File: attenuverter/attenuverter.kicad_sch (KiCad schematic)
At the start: 84 parts, among them J1 Power, J10 Conn_01x03_Socket, J11 Output 1, J12 Input 1, J13 Conn_01x03_Socket, J14 Conn_01x03_Socket, J15 Output 1, J16 Input 1, J17 Conn_01x03_Socket, J18 Conn_01x03_Socket, J19 Output 1, J2 Power, J3 Power, J4 Input 1, J5 Conn_01x03_Socket, J6 Conn_01x03_Socket, J7 Output 1, J8 Input 1, J9 Conn_01x03_Socket, U1 TL074, U2 TL074, U3 TL074

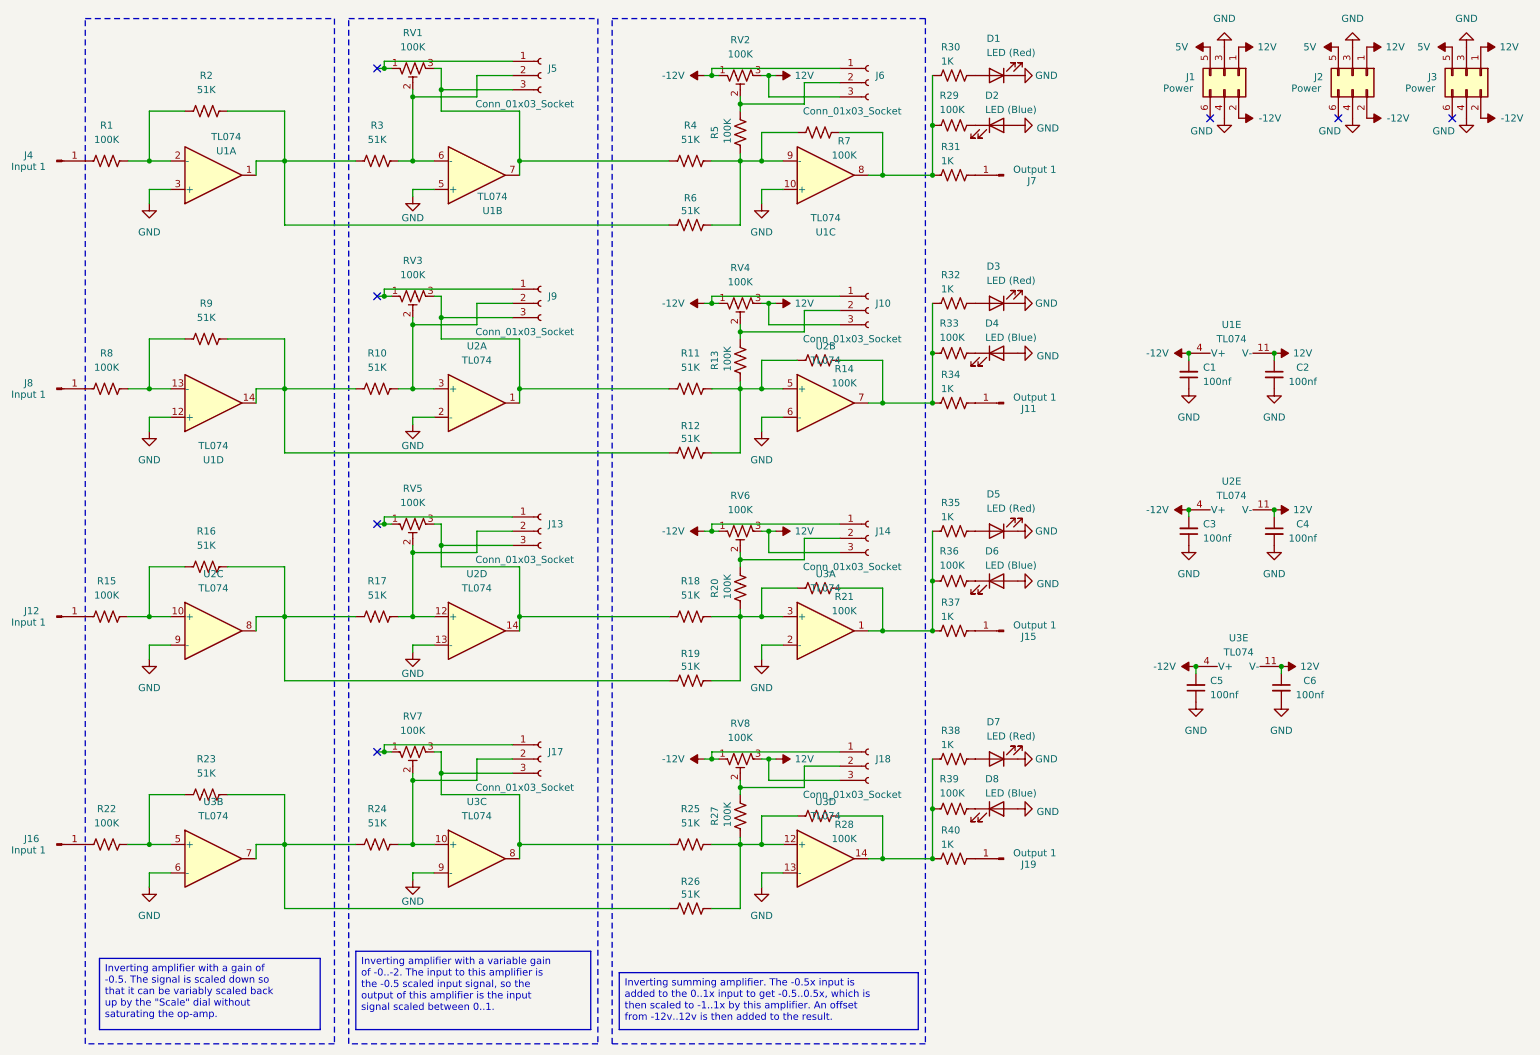
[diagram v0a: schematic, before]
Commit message: Fix attenuverter
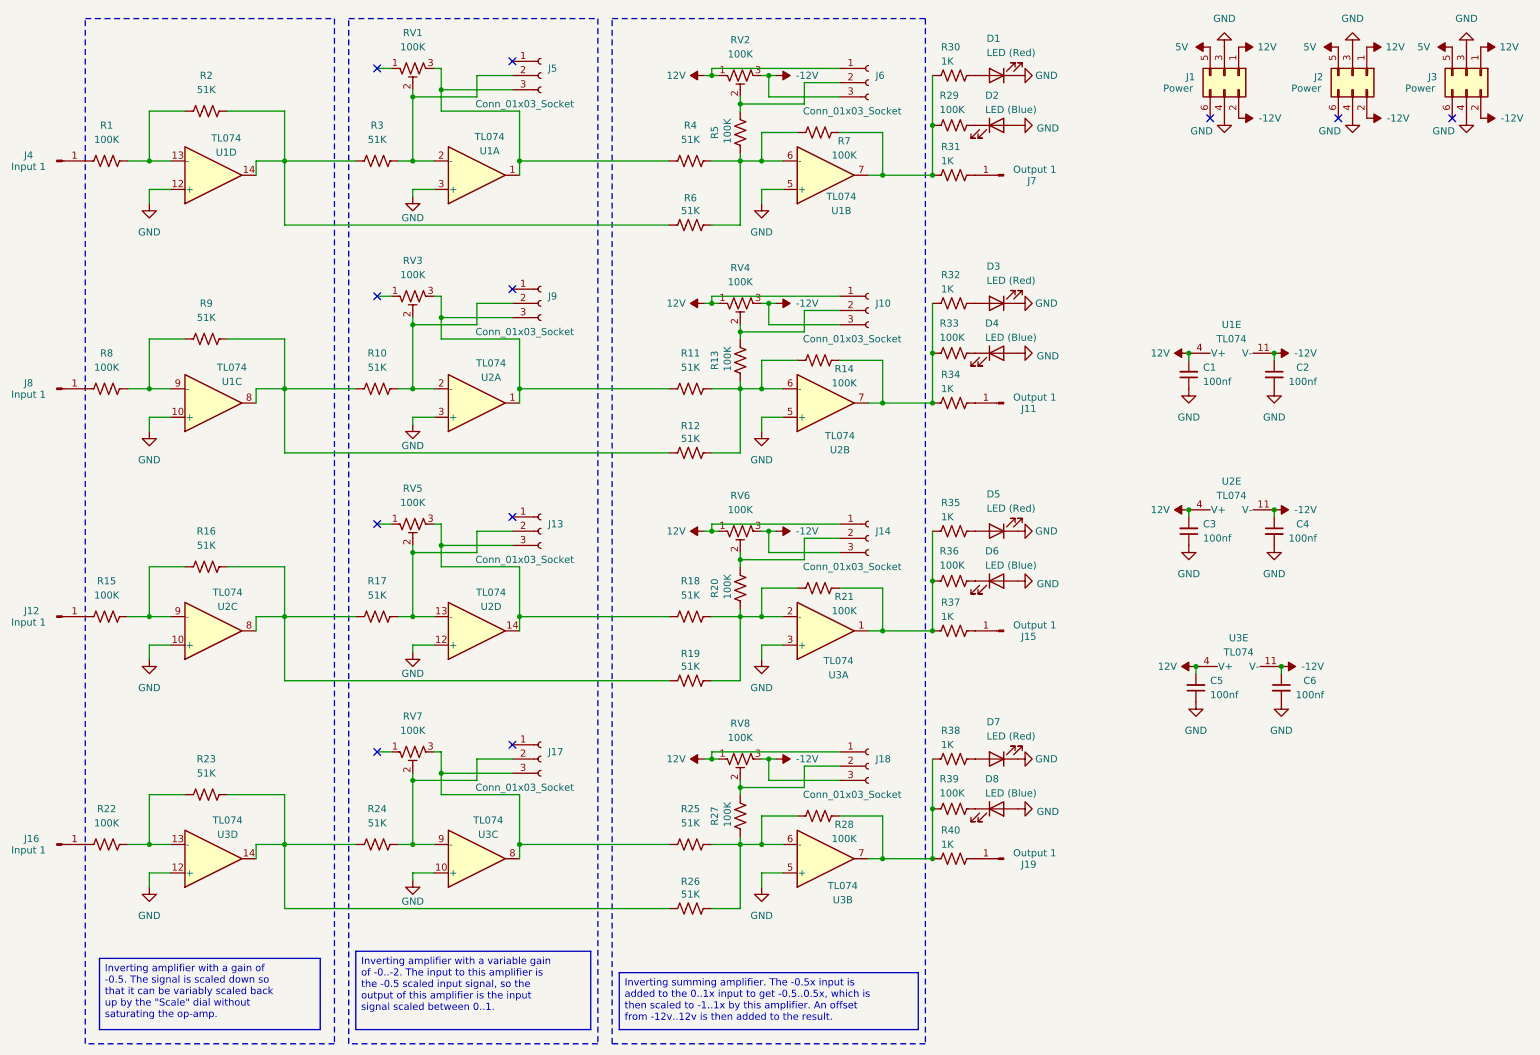
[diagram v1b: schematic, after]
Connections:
- net -12V: now also C2.1, C4.1, C6.1, J10.3 (Pin_3), J14.3 (Pin_3), J18.3 (Pin_3), J6.3 (Pin_3), RV2.3, RV4.3, RV6.3, RV8.3, U1.11 (V-), U2.11 (V-), U3.11 (V-); no longer C1.2, C3.2, C5.2, J10.1 (Pin_1), J14.1 (Pin_1), J18.1 (Pin_1), J6.1 (Pin_1), RV2.1, RV4.1, RV6.1, RV8.1, U1.4 (V+), U2.4 (V+), U3.4 (V+)
- net 12V: now also C1.2, C3.2, C5.2, J10.1 (Pin_1), J14.1 (Pin_1), J18.1 (Pin_1), J6.1 (Pin_1), RV2.1, RV4.1, RV6.1, RV8.1, U1.4 (V+), U2.4 (V+), U3.4 (V+); no longer C2.1, C4.1, C6.1, J10.3 (Pin_3), J14.3 (Pin_3), J18.3 (Pin_3), J6.3 (Pin_3), RV2.3, RV4.3, RV6.3, RV8.3, U1.11 (V-), U2.11 (V-), U3.11 (V-)
- net GND: now also U2.10 (+), U2.12 (+), U2.3 (+), U2.5 (+), U3.10 (+), U3.12 (+), U3.3 (+), U3.5 (+); no longer U2.13 (-), U2.2 (-), U2.6 (-), U2.9 (-), U3.13 (-), U3.2 (-), U3.6 (-), U3.9 (-)
- net at RV5.1: no longer J13.1 (Pin_1)
- net at J13.2 (Pin_2), R17.2, RV5.2: now also U2.13 (-); no longer U2.12 (+)
- net at R2.2, R3.1, R6.1: now also U1.14; no longer U1.1
- net at R1.2, R2.1: now also U1.13 (-); no longer U1.2 (-)
- net at R11.2, R12.2, R13.1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: now also U2.6 (-); no longer U2.5 (+)
- net at R25.2, R26.2, R27.1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: now also U3.6 (-); no longer U3.12 (+)
- net at R28.2, R38.2, R39.1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: now also U3.7; no longer U3.14
- net at R10.1, R12.1, R9.2: now also U1.8; no longer U1.14
- net at J17.2 (Pin_2), R24.2, RV7.2: now also U3.9 (-); no longer U3.10 (+)
- net at R8.2, R9.1: now also U1.9 (-); no longer U1.13 (-)
- net at R22.2, R23.1: now also U3.13 (-); no longer U3.5 (+)
- net at R23.2, R24.1, R26.1: now also U3.14; no longer U3.7
- net at R18.2, R19.2, R20.1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: now also U3.2 (-); no longer U3.3 (+)
- net at J5.2 (Pin_2), R3.2, RV1.2: now also U1.2 (-); no longer U1.6 (-)
- net at J5.3 (Pin_3), R4.1, RV1.3: now also U1.1; no longer U1.7
- net at R4.2, R5.1, R6.2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: now also U1.6 (-); no longer U1.9 (-)
- net at J9.2 (Pin_2), R10.2, RV3.2: now also U2.2 (-); no longer U2.3 (+)
- net at RV1.1: no longer J5.1 (Pin_1)
- net at R29.1, R30.2, R31.2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: now also U1.7; no longer U1.8
- net at RV3.1: no longer J9.1 (Pin_1)
- net at RV7.1: no longer J17.1 (Pin_1)
- net at R15.2, R16.1: now also U2.9 (-); no longer U2.10 (+)
- no-connect marks 7 -> 11
